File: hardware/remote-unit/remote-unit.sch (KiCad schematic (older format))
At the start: 48 parts, among them J1 SOL_A, J2 RF Module, J3 ICSP, J4 IO, J5 SOL_B, J6 PWR 12V, J7 UART, J8 I2C, SW1 RESET, U1 ATmega328P-AU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

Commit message: Update inductor footprint on remote unit
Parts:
- J2: footprint Connector_PinSocket_2.54mm:PinSocket_1x07_P2.54mm_Vertical -> lib:YL_800T
- L1: footprint Capacitor_THT:C_Radial_D5.0mm_H7.0mm_P2.00mm -> Inductor_SMD:L_12x12mm_H8mm; JLCPCB Part (none) -> C181844; Purchase Link https://au.mouser.com/ProductDetail/652-RLB0608-330KL -> NA
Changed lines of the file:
@@
 F 0 "L1" V 7440 950 50  0000 C CNN
 F 1 "33uH" V 7349 950 50  0000 C CNN
-F 2 "Capacitor_THT:C_Radial_D5.0mm_H7.0mm_P2.00mm" H 7250 950 50  0001 C CNN
-F 3 "https://au.mouser.com/datasheet/2/54/rlb-777833.pdf" H 7250 950 50  0001 C CNN
-F 4 "https://au.mouser.com/ProductDetail/652-RLB0608-330KL" H 7250 950 50  0001 C CNN "Purchase Link"
+F 2 "Inductor_SMD:L_12x12mm_H8mm" H 7250 950 50  0001 C CNN
+F 3 "https://datasheet.lcsc.com/lcsc/1810261033_Sunltech-Tech-SLH1207S330MTT_C181844.pdf" H 7250 950 50  0001 C CNN
+F 4 "NA" H 7250 950 50  0001 C CNN "Purchase Link"
+F 5 "C181844" H 7250 950 50  0001 C CNN "JLCPCB Part"
 	1    7250 950
 	0    -1   -1   0
@@
 F 0 "J2" V 9185 1728 50  0000 C CNN
 F 1 "RF Module" V 9276 1728 50  0000 C CNN
-F 2 "Connector_PinSocket_2.54mm:PinSocket_1x07_P2.54mm_Vertical" H 9350 1750 50  0001 C CNN
+F 2 "lib:YL_800T" H 9350 1750 50  0001 C CNN
 F 3 "~" H 9350 1750 50  0001 C CNN
 F 4 "https://au.element14.com/amphenol-icc/10129378-920003blf/conn-header-20pos-1row-2-54mm/dp/3728430" H 9350 1750 50  0001 C CNN "Purchase Link"

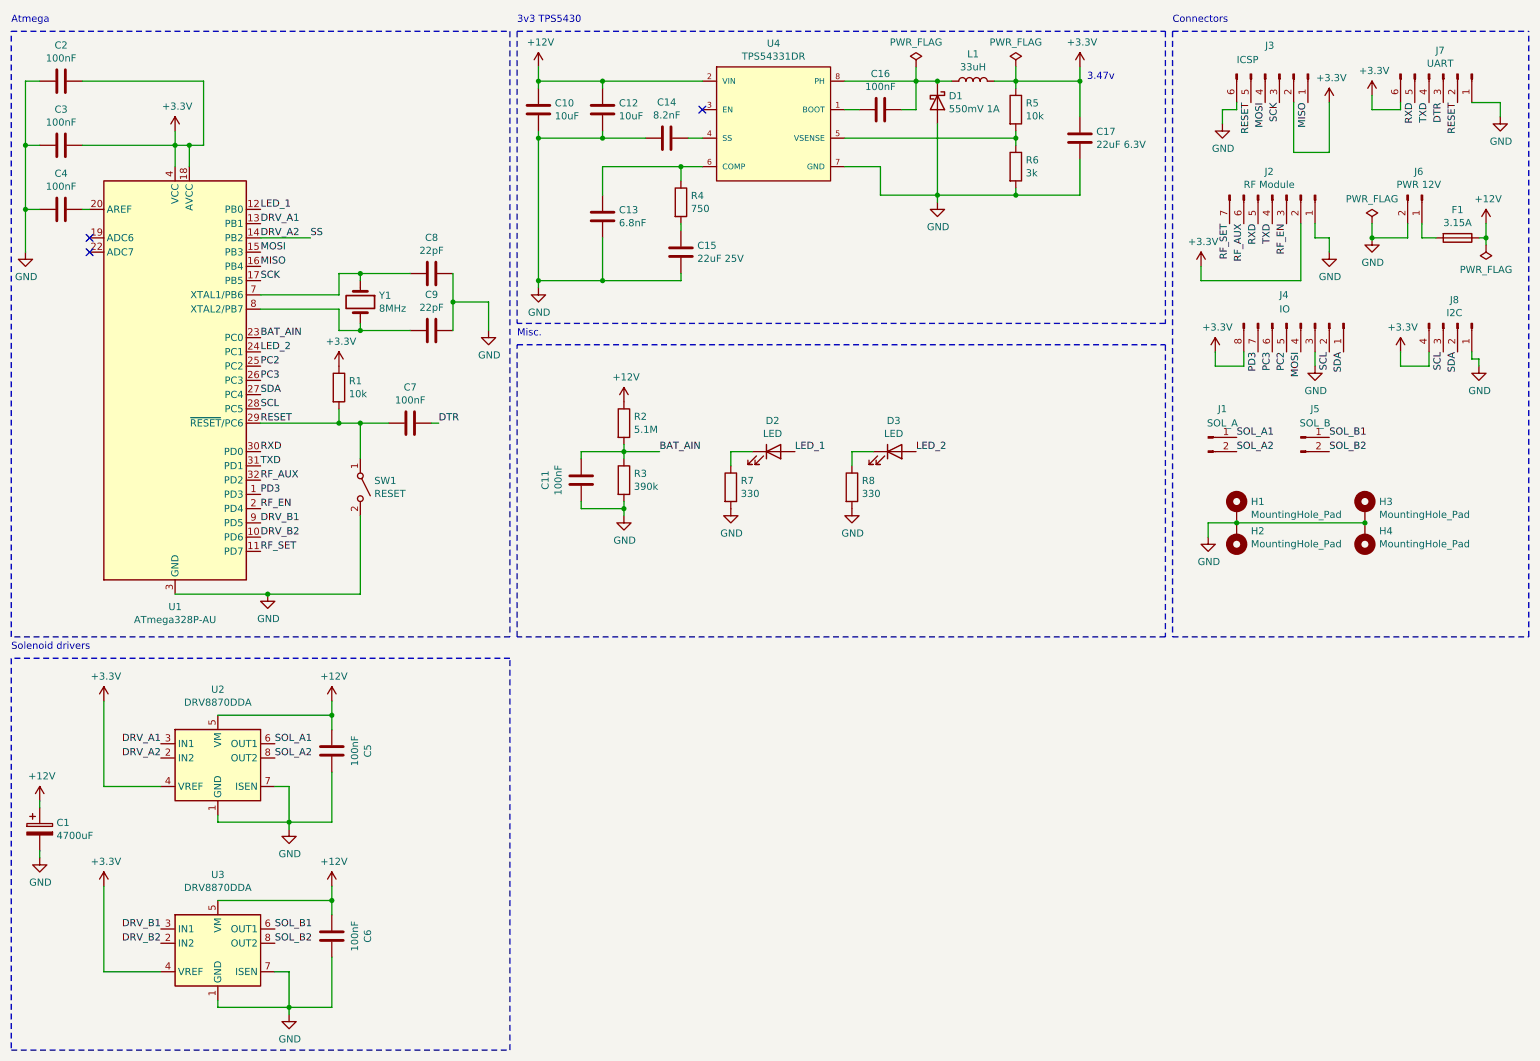
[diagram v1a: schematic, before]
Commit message: Add boost converter for solar panel
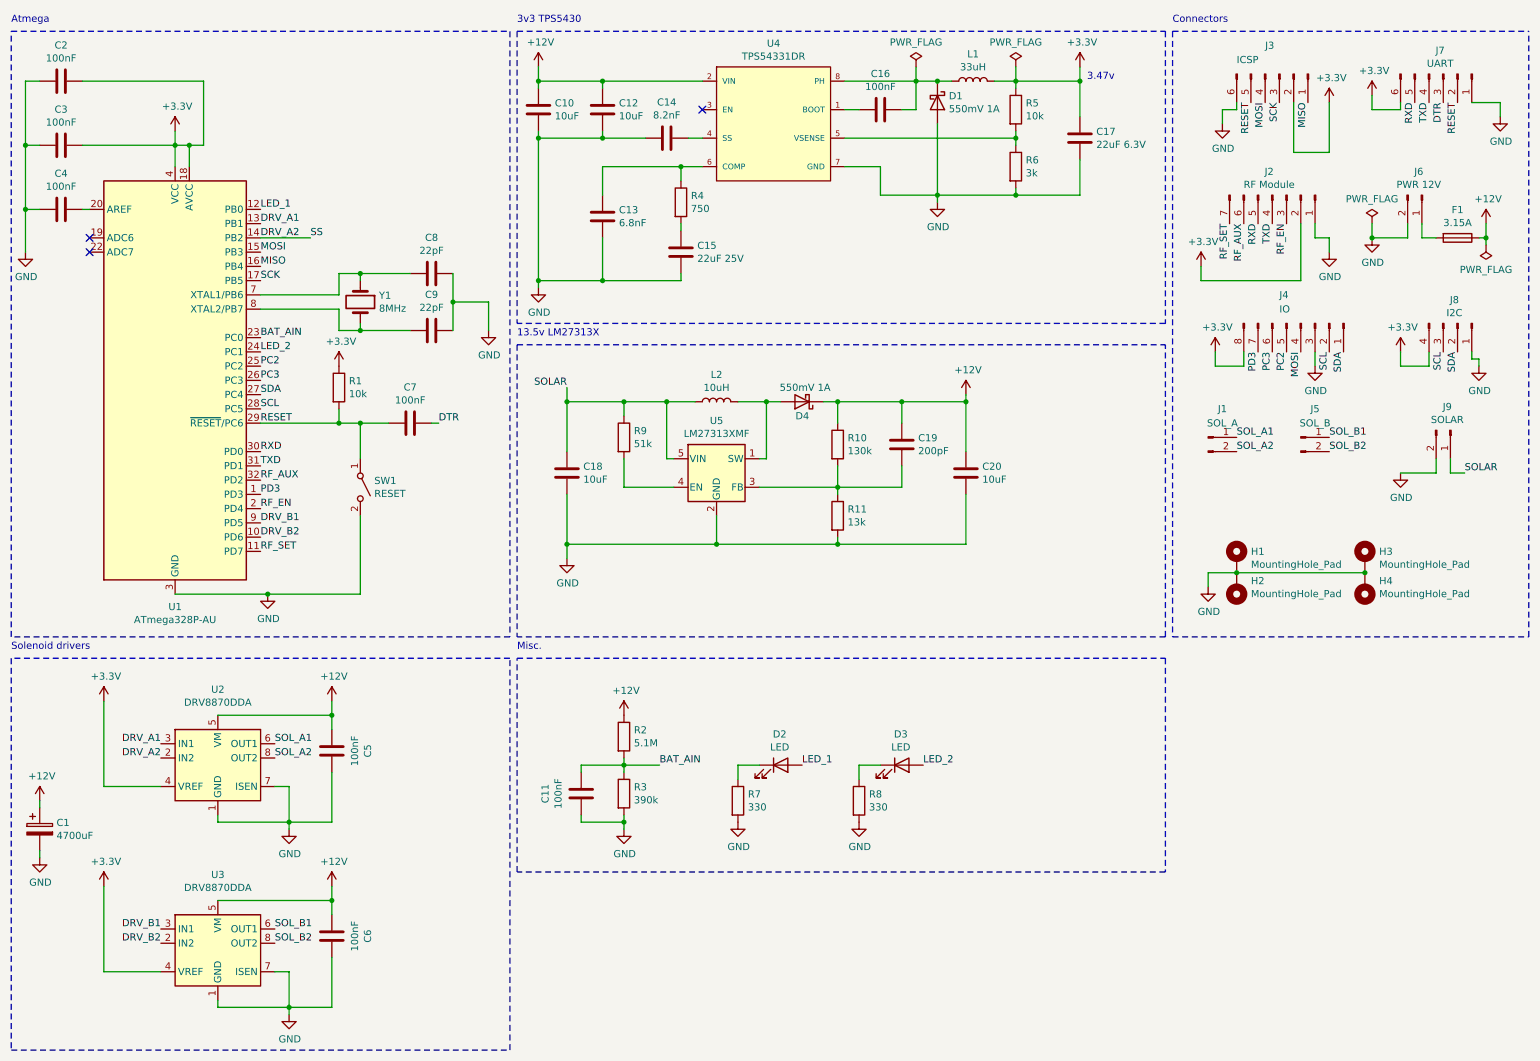
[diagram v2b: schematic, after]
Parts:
- added C18, C20: 10uF, Capacitor_SMD:C_1206_3216Metric, symbol Device:C
- added C19: 200pF, Capacitor_SMD:C_0603_1608Metric, symbol Device:C
- added D4: 550mV 1A, Diode_SMD:D_SMA, symbol Device:D_Schottky
- added J9: SOLAR, Connector_JST:JST_XH_B2B-XH-A_1x02_P2.50mm_Vertical, symbol Connector:Conn_01x02_Male
- added L2: 10uH, lib:L_4x4mm_H2mm, symbol Device:L
- added R10: 130k, Resistor_SMD:R_0603_1608Metric, symbol Device:R
- added R11: 13k, Resistor_SMD:R_0603_1608Metric, symbol Device:R
- added R9: 51k, Resistor_SMD:R_0402_1005Metric, symbol Device:R
- added U5: LM27313XMF, Package_TO_SOT_SMD:SOT-23-5, symbol Regulator_Switching:LM27313XMF
- L1: footprint Inductor_SMD:L_12x12mm_H8mm -> lib:L_8x8mm_H4mm; JLCPCB Part C181844 -> C253606; Purchase Link NA -> NA (Extended)
- U2, U3: Purchase Link NA -> NA (Extended)
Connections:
- net +12V: now also C19.1, C20.1, D4.1 (K), R10.1
- net GND: now also C18.2, C20.2, J9.2 (Pin_2), R11.2, U5.2 (GND)
- new net: D4.2 (A), L2.2, U5.1 (SW)
- new net: C19.2, R10.2, R11.1, U5.3 (FB)
- new net: R9.2, U5.4 (EN)
- new net SOLAR: C18.1, J9.1 (Pin_1), L2.1, R9.1, U5.5 (VIN)
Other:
- note added: "13.5v LM27313X"
- moved on the sheet: C11, D2, D3, H1, H2, H3, H4, R2, R3, R7, R8

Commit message: Fix remote unit buck converter
Compensation capacitor value was wrong.
Move output capacitor closer.
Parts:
- C15: value 22uF 25V -> 22nF 25V; footprint Capacitor_SMD:C_0805_2012Metric -> Capacitor_SMD:C_0603_1608Metric; JLCPCB Part C45783 -> C21122
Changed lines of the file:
@@
 P 5200 2150
 F 0 "C15" H 5315 2196 50  0000 L CNN
-F 1 "22uF 25V" H 5315 2105 50  0000 L CNN
-F 2 "Capacitor_SMD:C_0805_2012Metric" H 5238 2000 50  0001 C CNN
-F 3 "https://datasheet.lcsc.com/lcsc/1811151152_Samsung-Electro-Mechanics-CL21A226MAQNNNE_C45783.pdf" H 5200 2150 50  0001 C CNN
-F 4 "C45783" H 5200 2150 50  0001 C CNN "JLCPCB Part"
+F 1 "22nF 25V" H 5315 2105 50  0000 L CNN
+F 2 "Capacitor_SMD:C_0603_1608Metric" H 5238 2000 50  0001 C CNN
+F 3 "https://datasheet.lcsc.com/lcsc/1811101610_Samsung-Electro-Mechanics-CL10B223KB8NNNC_C21122.pdf" H 5200 2150 50  0001 C CNN
+F 4 "C21122" H 5200 2150 50  0001 C CNN "JLCPCB Part"
 F 5 "NA" H 5200 2150 50  0001 C CNN "Purchase Link"
 	1    5200 2150
